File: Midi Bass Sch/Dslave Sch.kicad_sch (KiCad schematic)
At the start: 5 parts

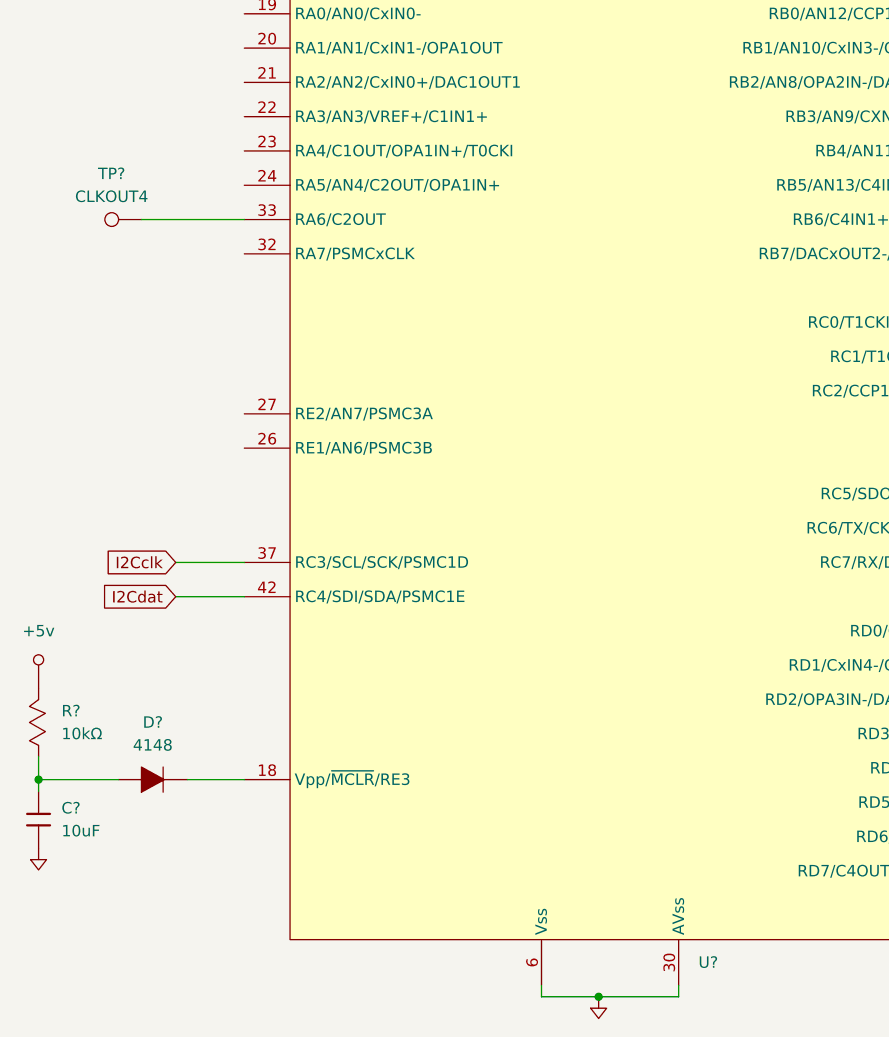
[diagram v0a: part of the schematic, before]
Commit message: updated e slave added solenoid for slave added reset button
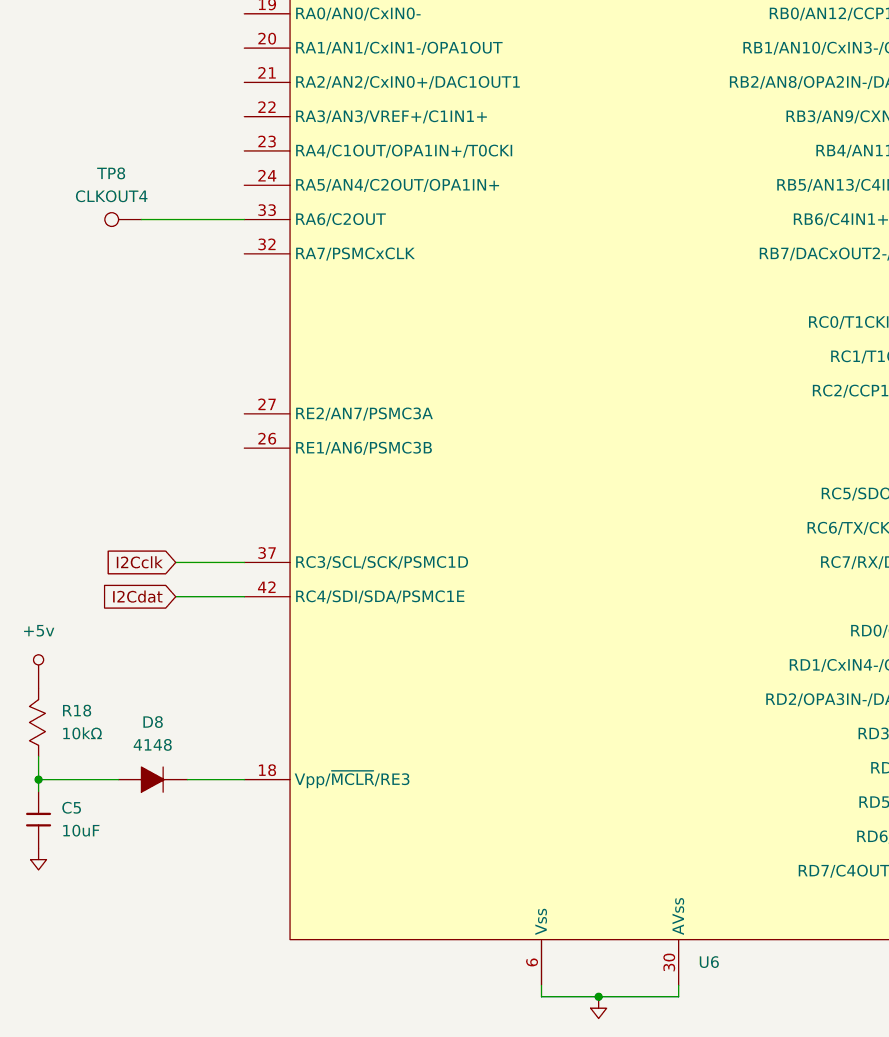
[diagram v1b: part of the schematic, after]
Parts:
- gave numbers to parts that had none: 5
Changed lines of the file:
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@@
 		(dnp no)
 		(fields_autoplaced yes)
-		(property "Reference" "U?"
+		(property "Reference" "U6"
 			(at 146.9741 158.75 0)
 			(effects
@@
 			(project "Midi Bass Sch"
 				(path "/06818073-fb22-48ee-acc5-6dedd827034e/4e89443f-252f-4d60-96aa-3cd5b0237902"
-					(reference "U?")
+					(reference "U6")
 					(unit 1)
 				)
@@
 		(dnp no)
 		(fields_autoplaced yes)
-		(property "Reference" "R?"
+		(property "Reference" "R18"
 			(at 76.2 130.8099 90)
 			(effects
@@
 			(project "Midi Bass Sch"
 				(path "/06818073-fb22-48ee-acc5-6dedd827034e/4e89443f-252f-4d60-96aa-3cd5b0237902"
-					(reference "R?")
+					(reference "R18")
 					(unit 1)
 				)
@@
 		(dnp no)
 		(fields_autoplaced yes)
-		(property "Reference" "TP?"
+		(property "Reference" "TP8"
 			(at 81.788 71.12 90)
 			(effects
@@
 			(project "Midi Bass Sch"
 				(path "/06818073-fb22-48ee-acc5-6dedd827034e/4e89443f-252f-4d60-96aa-3cd5b0237902"
-					(reference "TP?")
+					(reference "TP8")
 					(unit 1)
 				)
@@
 		(dnp no)
 		(fields_autoplaced yes)
-		(property "Reference" "D?"
+		(property "Reference" "D8"
 			(at 86.36 132.08 90)
 			(effects
@@
 			(project "Midi Bass Sch"
 				(path "/06818073-fb22-48ee-acc5-6dedd827034e/4e89443f-252f-4d60-96aa-3cd5b0237902"
-					(reference "D?")
+					(reference "D8")
 					(unit 1)
 				)
@@
 		(dnp no)
 		(fields_autoplaced yes)
-		(property "Reference" "C?"
+		(property "Reference" "C5"
 			(at 76.2 141.6049 0)
 			(effects
@@
 			(project "Midi Bass Sch"
 				(path "/06818073-fb22-48ee-acc5-6dedd827034e/4e89443f-252f-4d60-96aa-3cd5b0237902"
-					(reference "C?")
-					(unit 1)
-				)
+					(reference "C5")
+					(unit 1)
+				)

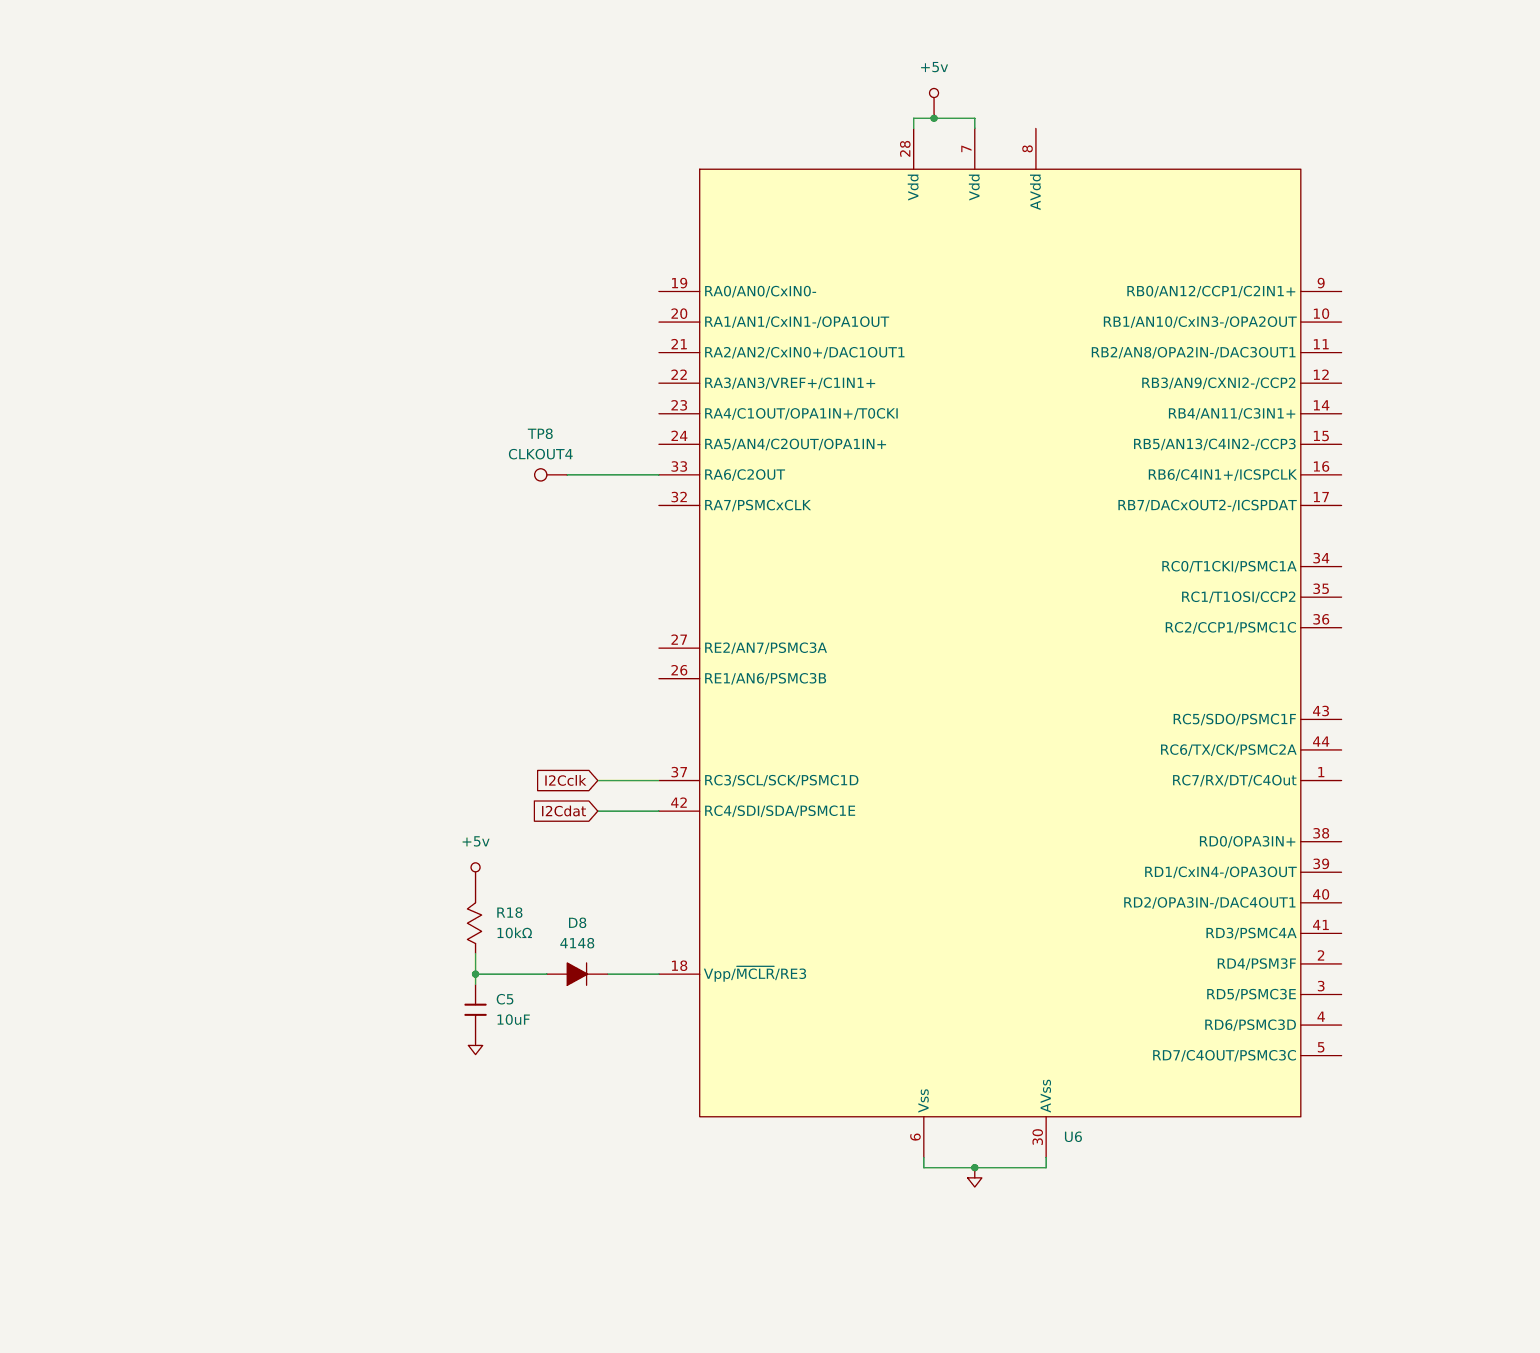
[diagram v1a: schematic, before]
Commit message: added solenoid array for the A slave
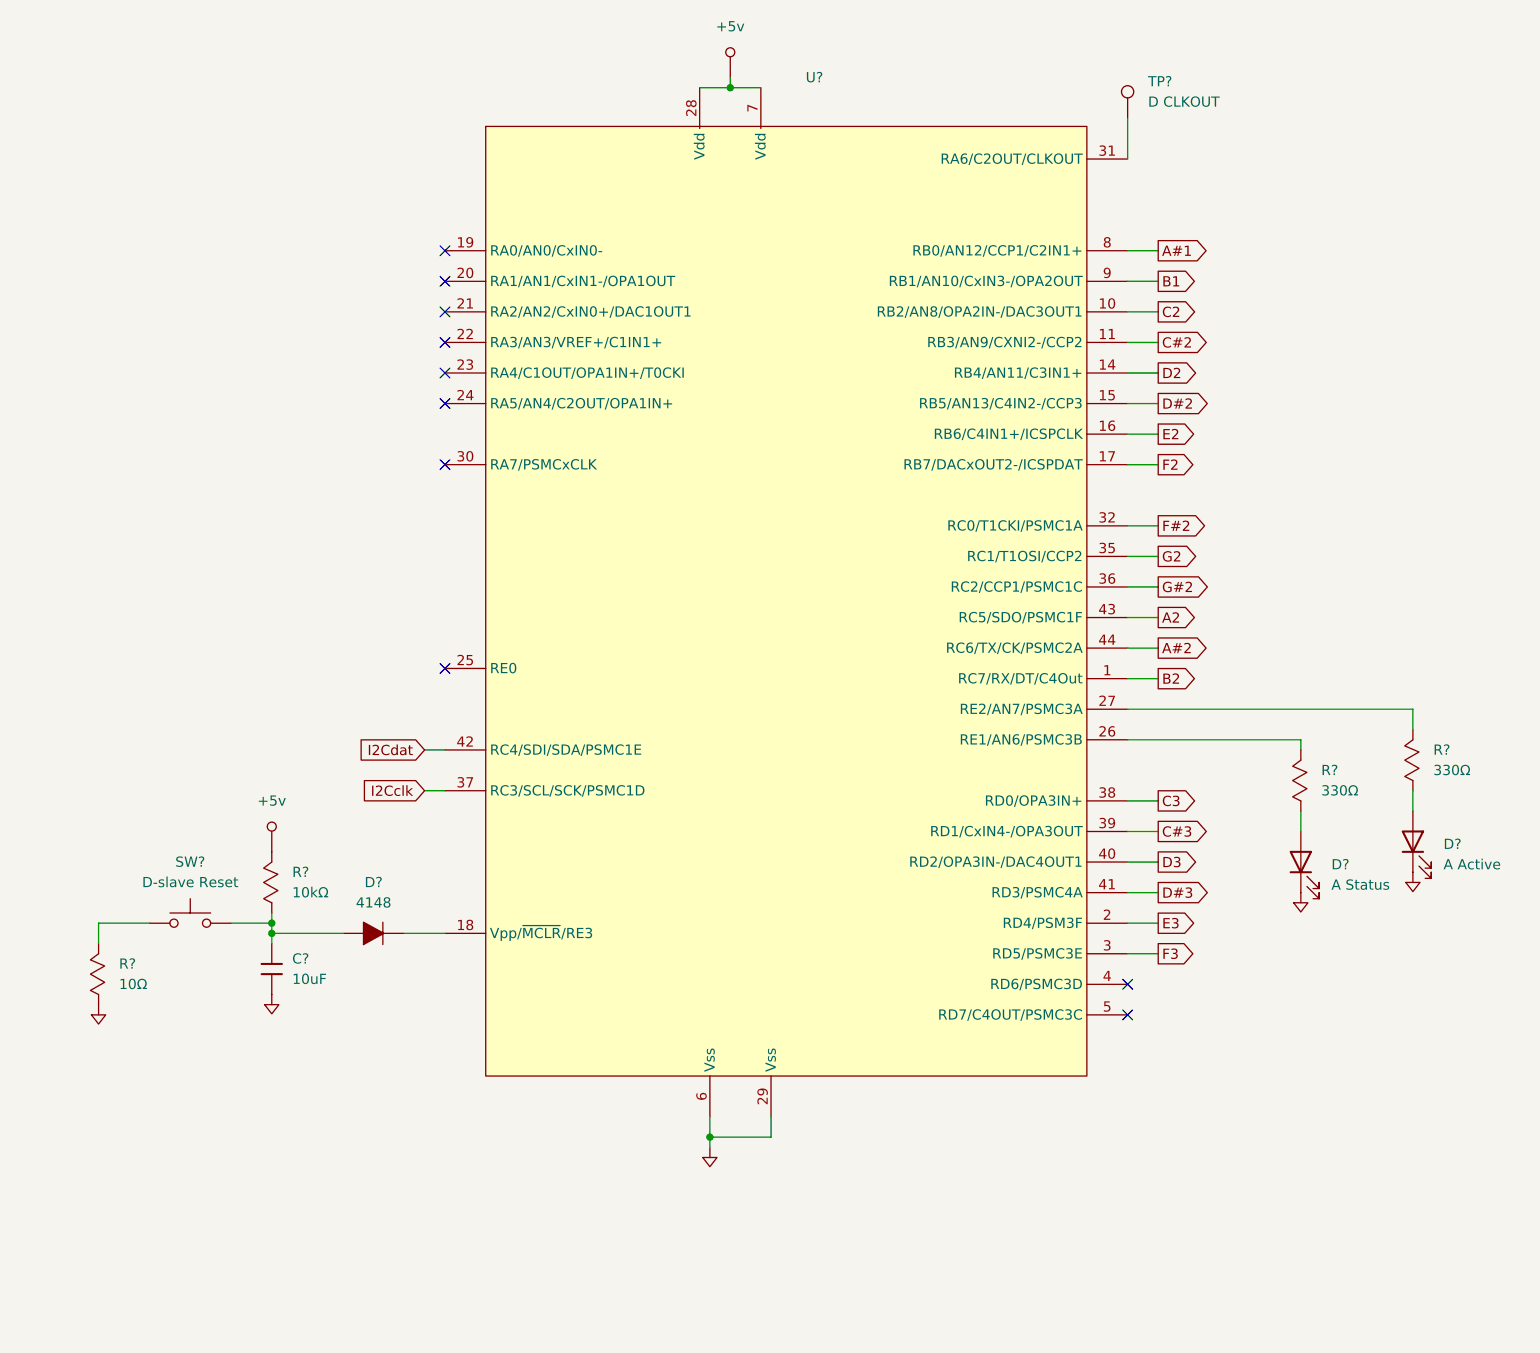
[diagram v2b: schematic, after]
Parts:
- removed C5: 10uF, symbol Owen's Symbols:Capacitor
- removed D8: 4148, symbol Owen's Symbols:Diode
- removed R18: 10kΩ, symbol Owen's Symbols:Resistor_Mod
- removed TP8: CLKOUT4, symbol Connector:TestPoint
- removed U6: ~, symbol Owen's Symbols:PIC16F1789_44
- added C?: 10uF, symbol Owen's Symbols:Capacitor
- added D?: A Status, symbol Device:LED
- added D?: A Active, symbol Device:LED
- added D?: 4148, symbol Owen's Symbols:Diode
- added R?: 10kΩ, symbol Owen's Symbols:Resistor_Mod
- added R? (x2): 330Ω, symbol Owen's Symbols:Resistor_Mod
- added R?: 10Ω, symbol Owen's Symbols:Resistor_Mod
- added SW?: D-slave Reset, symbol Switch:SW_Push
- added TP?: D CLKOUT, symbol Connector:TestPoint
- added U?: ~, symbol Owen's Symbols:PIC16F1789_44
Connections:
- net +5v: now also R?.2, U?.28 (Vdd), U?.7 (Vdd)
- net GND: now also C?.2, D?.1 (K), D?.1 (K), R?.1, U?.29 (Vss), U?.6 (Vss)
- new net: TP?.1, U?.31 (RA6/C2OUT/CLKOUT)
- new net: C?.1, D?.1, R?.1, SW?.2
- new net: R?.2, U?.1 (RC7/RX/DT/C4Out)
- new net: D?.2, U?.18 (Vpp/~{MCLR}/RE3)
- new net: R?.2, U?.44 (RC6/TX/CK/PSMC2A)
- new net: D?.2 (A), R?.1 (x2)
- new net: R?.2, SW?.1
- new net A#1: U?.8 (RB0/AN12/CCP1/C2IN1+)
- new net A#2: U?.42 (RC4/SDI/SDA/PSMC1E)
- new net A2: U?.37 (RC3/SCL/SCK/PSMC1D)
- new net B1: U?.9 (RB1/AN10/CxIN3-/OPA2OUT)
- new net B2: U?.43 (RC5/SDO/PSMC1F)
- new net C#2: U?.11 (RB3/AN9/CXNI2-/CCP2)
- new net C#3: U?.39 (RD1/CxIN4-/OPA3OUT)
- new net C2: U?.10 (RB2/AN8/OPA2IN-/DAC3OUT1)
- new net C3: U?.38 (RD0/OPA3IN+)
- new net D#2: U?.15 (RB5/AN13/C4IN2-/CCP3)
- new net D#3: U?.41 (RD3/PSMC4A)
- new net D2: U?.14 (RB4/AN11/C3IN1+)
- new net D3: U?.40 (RD2/OPA3IN-/DAC4OUT1)
- new net E2: U?.16 (RB6/C4IN1+/ICSPCLK)
- new net E3: U?.2 (RD4/PSM3F)
- new net F#2: U?.32 (RC0/T1CKI/PSMC1A)
- new net F2: U?.17 (RB7/DACxOUT2-/ICSPDAT)
- new net F3: U?.3 (RD5/PSMC3E)
- new net G#2: U?.36 (RC2/CCP1/PSMC1C)
- new net G2: U?.35 (RC1/T1OSI/CCP2)
- no-connect marks 0 -> 10

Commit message: added solenoid array for the D slave
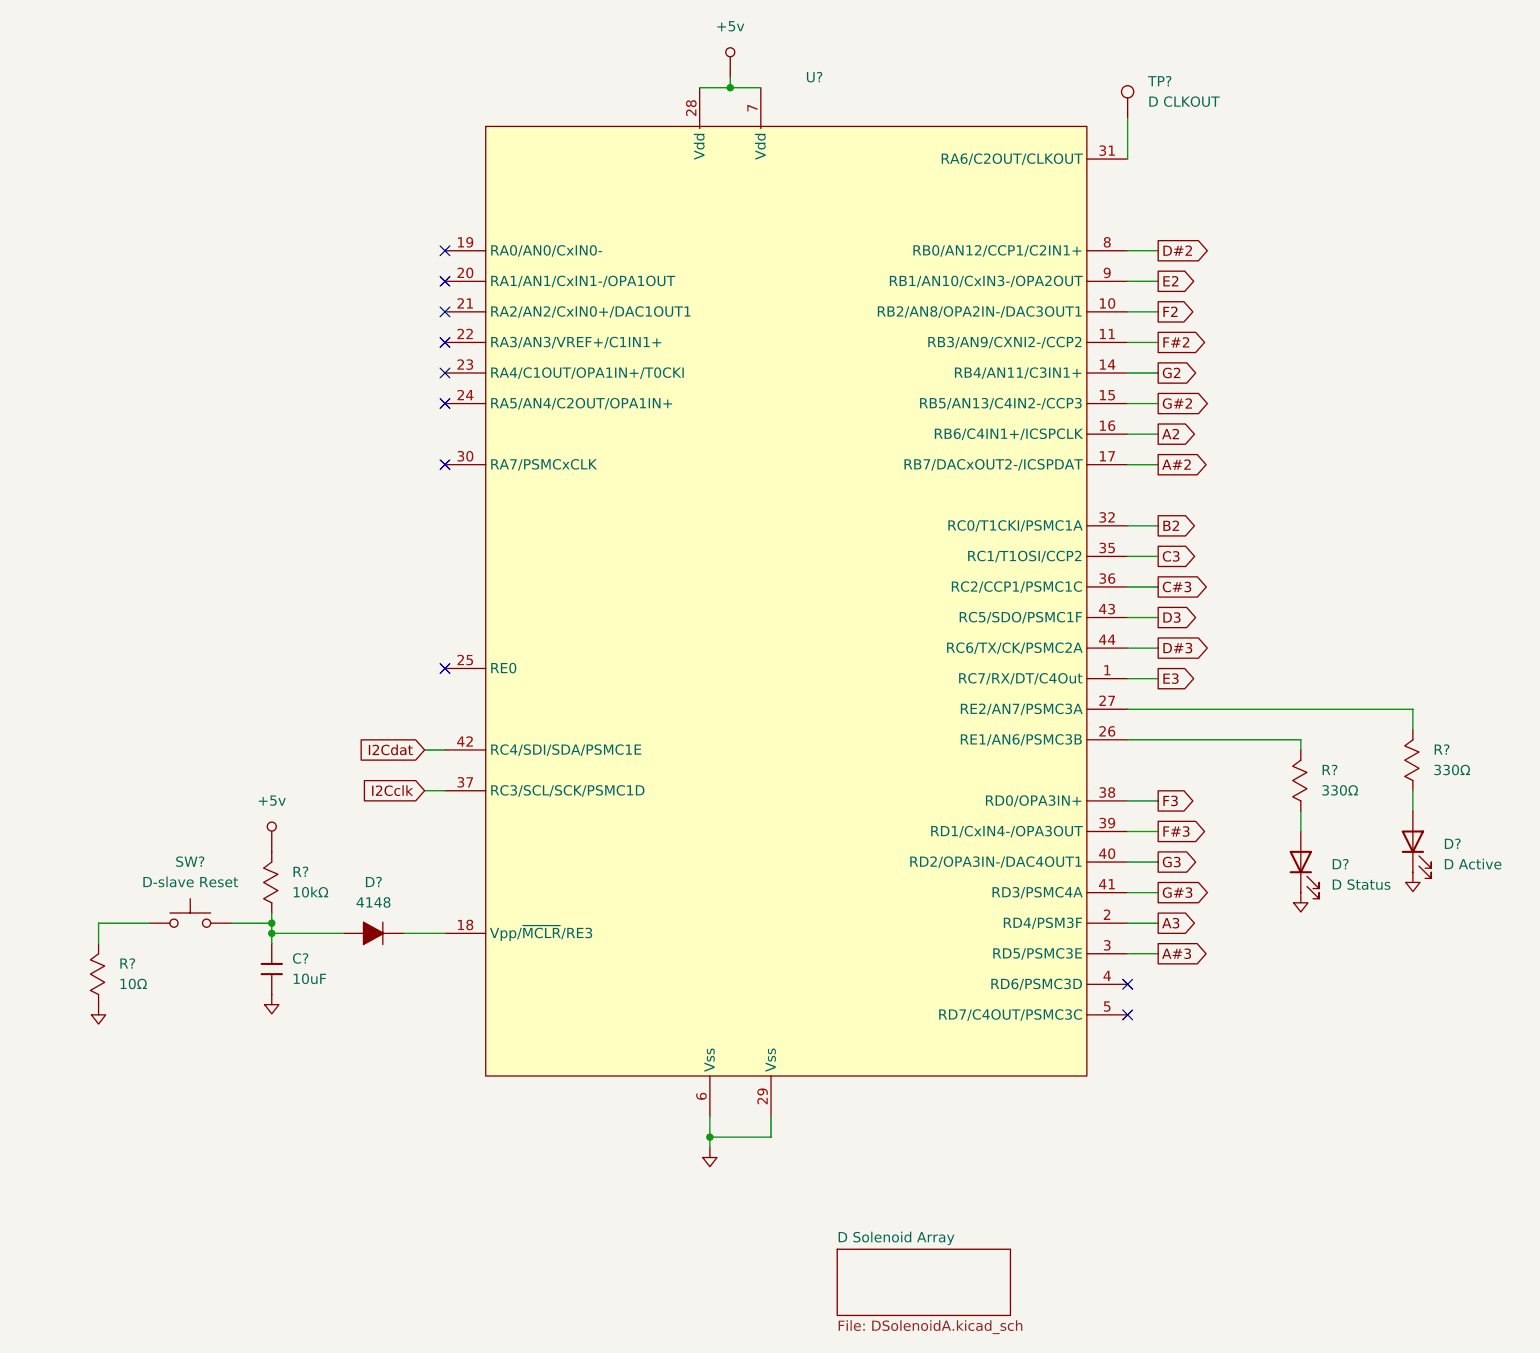
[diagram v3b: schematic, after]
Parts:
- D?: value A Status -> D Status
- D?: value A Active -> D Active
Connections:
- net A#1 is gone; now on net D#2: U?.8 (RB0/AN12/CCP1/C2IN1+)
- net B1 is gone; now on net E2: U?.9 (RB1/AN10/CxIN3-/OPA2OUT)
- net C#2 is gone; now on net F#2: U?.11 (RB3/AN9/CXNI2-/CCP2)
- net C2 is gone; now on net F2: U?.10 (RB2/AN8/OPA2IN-/DAC3OUT1)
- net D2 is gone; now on net G2: U?.14 (RB4/AN11/C3IN1+)
- net A#2: now also U?.17 (RB7/DACxOUT2-/ICSPDAT); no longer U?.42 (RC4/SDI/SDA/PSMC1E)
- net A2: now also U?.16 (RB6/C4IN1+/ICSPCLK); no longer U?.37 (RC3/SCL/SCK/PSMC1D)
- net B2: now also U?.32 (RC0/T1CKI/PSMC1A); no longer U?.43 (RC5/SDO/PSMC1F)
- net C#3: now also U?.36 (RC2/CCP1/PSMC1C); no longer U?.39 (RD1/CxIN4-/OPA3OUT)
- net C3: now also U?.35 (RC1/T1OSI/CCP2); no longer U?.38 (RD0/OPA3IN+)
- net D#2: no longer U?.15 (RB5/AN13/C4IN2-/CCP3)
- net D#3: now also U?.42 (RC4/SDI/SDA/PSMC1E); no longer U?.41 (RD3/PSMC4A)
- net D3: now also U?.37 (RC3/SCL/SCK/PSMC1D); no longer U?.40 (RD2/OPA3IN-/DAC4OUT1)
- net E2: no longer U?.16 (RB6/C4IN1+/ICSPCLK)
- net E3: now also U?.43 (RC5/SDO/PSMC1F); no longer U?.2 (RD4/PSM3F)
- net F#2: no longer U?.32 (RC0/T1CKI/PSMC1A)
- net F2: no longer U?.17 (RB7/DACxOUT2-/ICSPDAT)
- net F3: now also U?.38 (RD0/OPA3IN+); no longer U?.3 (RD5/PSMC3E)
- net G#2: now also U?.15 (RB5/AN13/C4IN2-/CCP3); no longer U?.36 (RC2/CCP1/PSMC1C)
- net G2: no longer U?.35 (RC1/T1OSI/CCP2)
- new net A#3: U?.3 (RD5/PSMC3E)
- new net A3: U?.2 (RD4/PSM3F)
- new net F#3: U?.39 (RD1/CxIN4-/OPA3OUT)
- new net G#3: U?.41 (RD3/PSMC4A)
- new net G3: U?.40 (RD2/OPA3IN-/DAC4OUT1)
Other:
- added sheet D Solenoid Array (DSolenoidA.kicad_sch)
